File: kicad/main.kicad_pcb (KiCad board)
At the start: 2 copper layers, 13 parts, among them J1 Conn_02x14_Counter_Clockwise, U1 7421, U2 74LS86, U3 74LS138, U4 7421, U5 7421, U6 74LS138

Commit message: started layout for multiplexer
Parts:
- moved C4 114.3 mm to (281.9, 76.2)
- moved C2 112.3 mm to (282.0, 99.1)
- moved C1 110.8 mm to (282.0, 85.1)
- moved C3 110.1 mm to (282.0, 92.7)
- moved C5 109.4 mm to (282.0, 106.7)
- moved C6 109.3 mm to (282.0, 111.8)
- moved U6 108.5 mm to (76.9, 160.3), turned to -90 degrees
- moved U3 90.2 mm to (59.2, 155.2), turned to 90 degrees
- moved J1 73.1 mm to (43.2, 97.8), turned to 180 degrees
- moved U5 43.2 mm to (129.5, 91.4)
- moved U4 22.6 mm to (129.5, 58.4)
- moved U1 19.0 mm to (147.3, 73.7)
- moved U2 6.85 mm to (86.4, 76.2)
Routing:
- net +5V: track 0.00 -> 70.0 mm
- net GND: track 0.00 -> 68.9 mm, vias 0 -> 1
- net /adressInverter//PWM: track 0.00 -> 56.4 mm
- net /adressInverter/H3_OUT: track 0.00 -> 46.6 mm
- net /adressInverter/H1_OUT: track 0.00 -> 35.1 mm
- net Net-(U6-~{Y6}): track 0.00 -> 26.1 mm
- net /adressInverter/H2_OUT: track 0.00 -> 25.6 mm
- net Net-(U6-~{Y5}): track 0.00 -> 23.9 mm
- net Net-(U6-~{Y4}): track 0.00 -> 21.6 mm
- net unconnected-(U3-~{Y0}-Pad15): track 0.00 -> 20.4 mm
- net Net-(U6-~{Y3}): track 0.00 -> 18.8 mm
- net Net-(U3-~{Y1}): track 0.00 -> 16.3 mm
- net /PWM_IN: track 0.00 -> 16.2 mm
- net Net-(U6-~{Y2}): track 0.00 -> 14.0 mm
- net Net-(U3-~{Y2}): track 0.00 -> 13.4 mm
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
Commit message: finished individual components layouts
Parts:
- moved C2 223.7 mm to (58.5, 88.9)
- moved C4 169.5 mm to (118.1, 119.7), turned to -90 degrees
- moved C1 153.2 mm to (141.0, 145.0)
- moved C6 126.7 mm to (163.8, 66.1), turned to 180 degrees
- moved C3 103.8 mm to (181.6, 66.0), turned to 180 degrees
- moved C5 92.0 mm to (199.4, 66.0)
- moved U5 68.2 mm to (191.8, 63.5), turned to 180 degrees
- moved U3 66.5 mm to (120.7, 129.8)
- moved U6 66.5 mm to (138.4, 134.9)
- moved U1 63.1 mm to (209.6, 63.5), turned to 180 degrees
- moved U4 44.7 mm to (174.0, 63.5), turned to 180 degrees
- moved U2 22.7 mm to (66.0, 86.4), turned to 180 degrees
- moved J1 10.5 mm to (53.3, 95.3)
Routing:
- net GND: track 68.9 -> 195.1 mm
- net +5V: track 70.0 -> 185.5 mm
- net Net-(U6-~{Y3}): track 18.8 -> 112.7 mm
- net /G_L_OUT: track 0.00 -> 72.9 mm
- net Net-(U3-~{Y5}): track 4.57 -> 71.8 mm
- net Net-(U3-~{Y4}): track 7.49 -> 70.2 mm
- net Net-(U6-~{Y2}): track 14.0 -> 71.6 mm
- net /B_L_OUT: track 0.00 -> 55.5 mm
- net /Y_H_OUT: track 0.00 -> 51.2 mm
- net Net-(U3-~{Y2}): track 13.4 -> 61.3 mm
- net Net-(U6-~{Y5}): track 23.9 -> 71.1 mm
- net Net-(U3-~{Y6}): track 4.42 -> 49.8 mm
- net Net-(U6-~{Y1}): track 11.2 -> 42.9 mm
- net /PWM_IN: track 16.2 -> 43.4 mm
- net /H1_IN: track 0.00 -> 23.6 mm
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
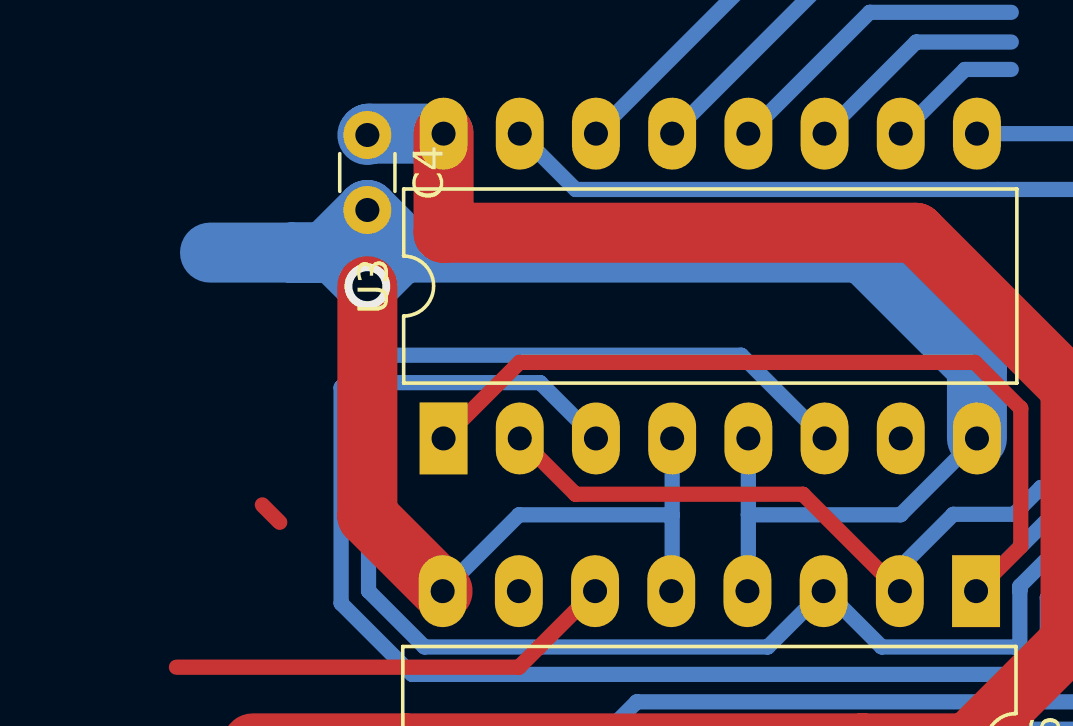
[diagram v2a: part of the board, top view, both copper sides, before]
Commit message: deleted unnecessary complexity
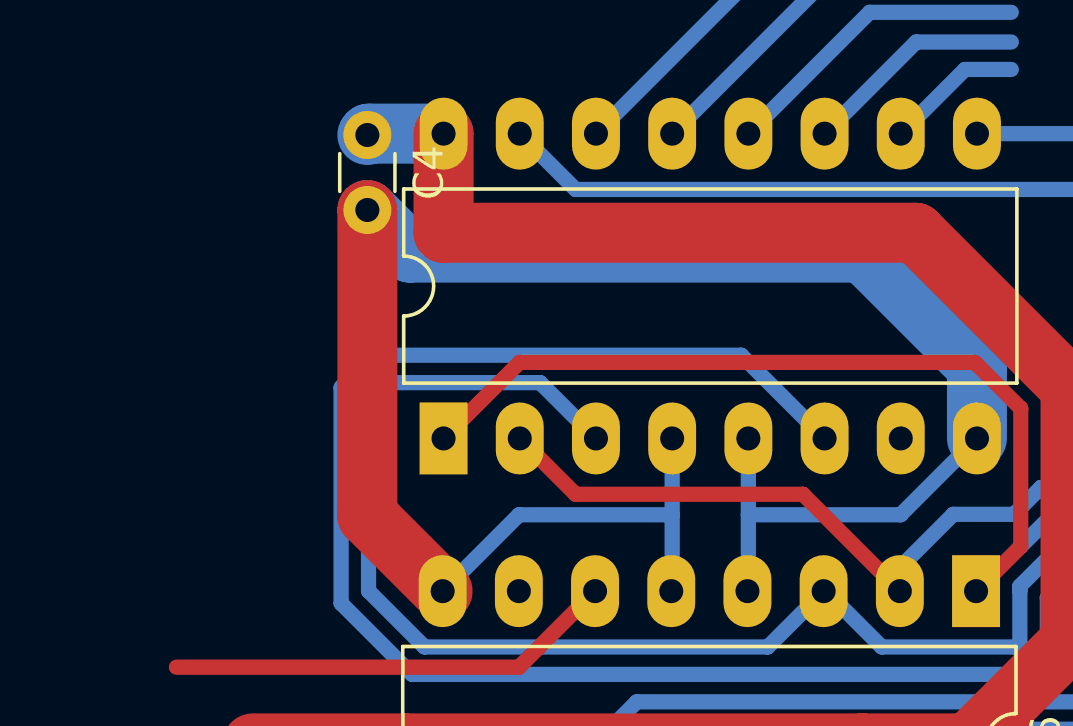
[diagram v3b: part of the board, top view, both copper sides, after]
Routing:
- net GND: track 195.1 -> 187.0 mm, vias 1 -> 0
- net /PWM_IN: track 43.4 -> 42.5 mm
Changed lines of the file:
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@@
     (property "Sheetname" "com_dmux")
     (attr through_hole)
-    (fp_text reference "U3" (at 5.08 -2.33 90) (layer "F.SilkS")
+    (fp_text reference "U3" (at 5.08 -2.33 90) (layer "F.SilkS") hide
         (effects (font (size 1 1) (thickness 0.15)))
     )
@@
   (segment (start 181.62 66.045) (end 181.62 66.665321) (width 2) (layer "B.Cu") (net 1))
   (segment (start 140.981578 145.0248) (end 140.986578 145.0198) (width 2) (layer "B.Cu") (net 1))
-  (segment (start 118.126578 124.6998) (end 118.126578 132.3548) (width 2) (layer "F.Cu") (net 2))
   (segment (start 177.299999 58.44) (end 177.299999 49.224999) (width 2) (layer "F.Cu") (net 2))
+  (segment (start 118.126578 122.1598) (end 118.126578 132.3548) (width 2) (layer "F.Cu") (net 2))
   (segment (start 179.12 66.045) (end 177.299999 64.224999) (width 2) (layer "F.Cu") (net 2))
   (segment (start 118.126578 132.3548) (end 120.636578 134.8648) (width 2) (layer "F.Cu") (net 2))
@@
   (segment (start 176.54 48.465) (end 174 48.465) (width 2) (layer "F.Cu") (net 2))
   (segment (start 177.299999 49.224999) (end 176.54 48.465) (width 2) (layer "F.Cu") (net 2))
-  (via (at 118.126578 124.6998) (size 1.524) (drill 1) (layers "F.Cu" "B.Cu") (net 2))
   (segment (start 201.94 46.0536) (end 202.0014 46.115) (width 2) (layer "B.Cu") (net 2))
   (segment (start 63.1096 84.50776) (end 63.1096 73.060079) (width 2) (layer "B.Cu") (net 2))
-  (segment (start 119.246578 123.2798) (end 119.246578 123.5798) (width 2) (layer "B.Cu") (net 2))
   (segment (start 201.94 46.0536) (end 207.3436 46.0536) (width 2) (layer "B.Cu") (net 2))
+  (segment (start 118.126578 122.1598) (end 119.546578 123.5798) (width 2) (layer "B.Cu") (net 2))
   (segment (start 66.03 86.36) (end 64.96184 86.36) (width 2) (layer "B.Cu") (net 2))
   (segment (start 193.9764 46.0536) (end 201.94 46.0536) (width 2) (layer "B.Cu") (net 2))
-  (segment (start 115.586578 123.5798) (end 112.881578 123.5798) (width 2) (layer "B.Cu") (net 2))
   (segment (start 130.826578 132.3198) (end 130.826578 134.8348) (width 0.508) (layer "B.Cu") (net 2))
   (segment (start 60.96 88.9) (end 63.1096 86.7504) (width 2) (layer "B.Cu") (net 2))
@@
   (segment (start 57.155 62.245) (end 66.03 71.12) (width 2) (layer "B.Cu") (net 2))
   (segment (start 64.716079 71.4536) (end 66.04 71.4536) (width 2) (layer "B.Cu") (net 2))
-  (segment (start 118.126578 122.1598) (end 119.246578 123.2798) (width 2) (layer "B.Cu") (net 2))
   (segment (start 128.286578 129.7748) (end 128.286578 132.3198) (width 0.508) (layer "B.Cu") (net 2))
   (segment (start 176.1964 46.0686) (end 174 48.265) (width 2) (layer "B.Cu") (net 2))
@@
   (segment (start 135.901578 132.3198) (end 130.826578 132.3198) (width 0.508) (layer "B.Cu") (net 2))
   (segment (start 134.651578 123.5798) (end 138.446578 127.3748) (width 2) (layer "B.Cu") (net 2))
-  (segment (start 118.126578 122.1598) (end 116.706578 123.5798) (width 2) (layer "B.Cu") (net 2))
+  (segment (start 119.546578 123.5798) (end 134.651578 123.5798) (width 2) (layer "B.Cu") (net 2))
   (segment (start 191.77 48.26) (end 189.5636 46.0536) (width 2) (layer "B.Cu") (net 2))
   (segment (start 120.636578 134.8648) (end 123.181578 132.3198) (width 0.508) (layer "B.Cu") (net 2))
-  (segment (start 116.706578 123.5798) (end 115.586578 123.5798) (width 2) (layer "B.Cu") (net 2))
   (segment (start 63.1096 73.060079) (end 64.716079 71.4536) (width 2) (layer "B.Cu") (net 2))
   (segment (start 128.286578 132.3198) (end 128.286578 134.8348) (width 0.508) (layer "B.Cu") (net 2))
-  (segment (start 118.126578 124.6998) (end 119.246578 123.5798) (width 2) (layer "B.Cu") (net 2))
   (segment (start 202.0014 46.115) (end 202.0014 65.9436) (width 2) (layer "B.Cu") (net 2))
   (segment (start 189.5636 46.0536) (end 176.1964 46.0536) (width 2) (layer "B.Cu") (net 2))
-  (segment (start 117.006578 123.5798) (end 115.586578 123.5798) (width 2) (layer "B.Cu") (net 2))
-  (segment (start 118.126578 124.6998) (end 117.006578 123.5798) (width 2) (layer "B.Cu") (net 2))
   (segment (start 191.77 48.26) (end 193.9764 46.0536) (width 2) (layer "B.Cu") (net 2))
   (segment (start 138.446578 129.7748) (end 135.901578 132.3198) (width 0.508) (layer "B.Cu") (net 2))
@@
   (segment (start 64.96184 86.36) (end 63.1096 84.50776) (width 2) (layer "B.Cu") (net 2))
   (segment (start 53.345 62.245) (end 57.155 62.245) (width 2) (layer "B.Cu") (net 2))
-  (segment (start 119.246578 123.5798) (end 134.651578 123.5798) (width 2) (layer "B.Cu") (net 2))
   (segment (start 207.3436 46.0536) (end 209.55 48.26) (width 2) (layer "B.Cu") (net 2))
   (segment (start 202.0014 65.9436) (end 201.9 66.045) (width 2) (layer "B.Cu") (net 2))
@@
   (segment (start 123.856178 136.7252) (end 123.181578 137.3998) (width 0.508) (layer "F.Cu") (net 8))
   (segment (start 66.938 83.82) (end 66.03 83.82) (width 0.508) (layer "F.Cu") (net 8))
-  (segment (start 115.206778 132.5704) (end 114.626378 131.99) (width 0.508) (layer "F.Cu") (net 8))
   (segment (start 125.716578 134.8648) (end 125.716578 134.4648) (width 0.508) (layer "F.Cu") (net 8))
   (segment (start 56.5496 89.054918) (end 58.055082 90.5604) (width 0.508) (layer "B.Cu") (net 8))

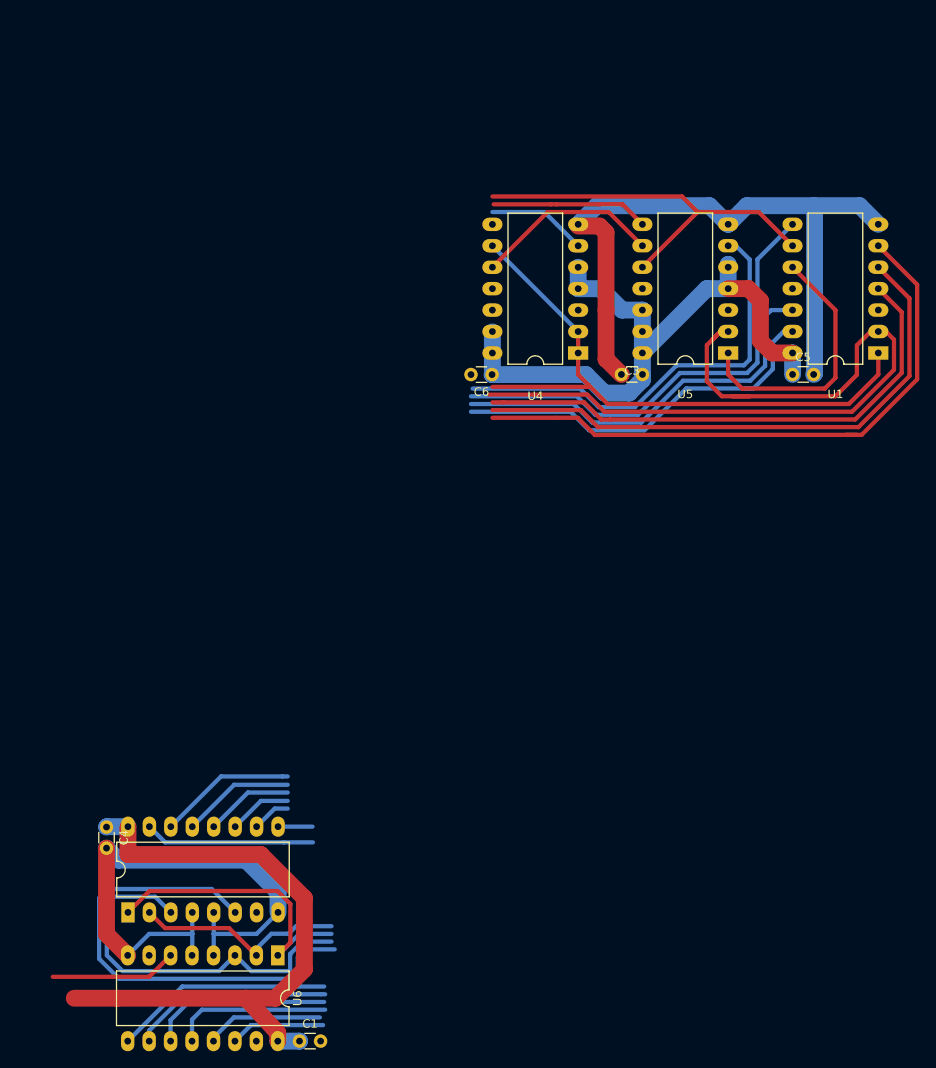
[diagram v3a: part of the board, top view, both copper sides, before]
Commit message: fixed unreachable pin
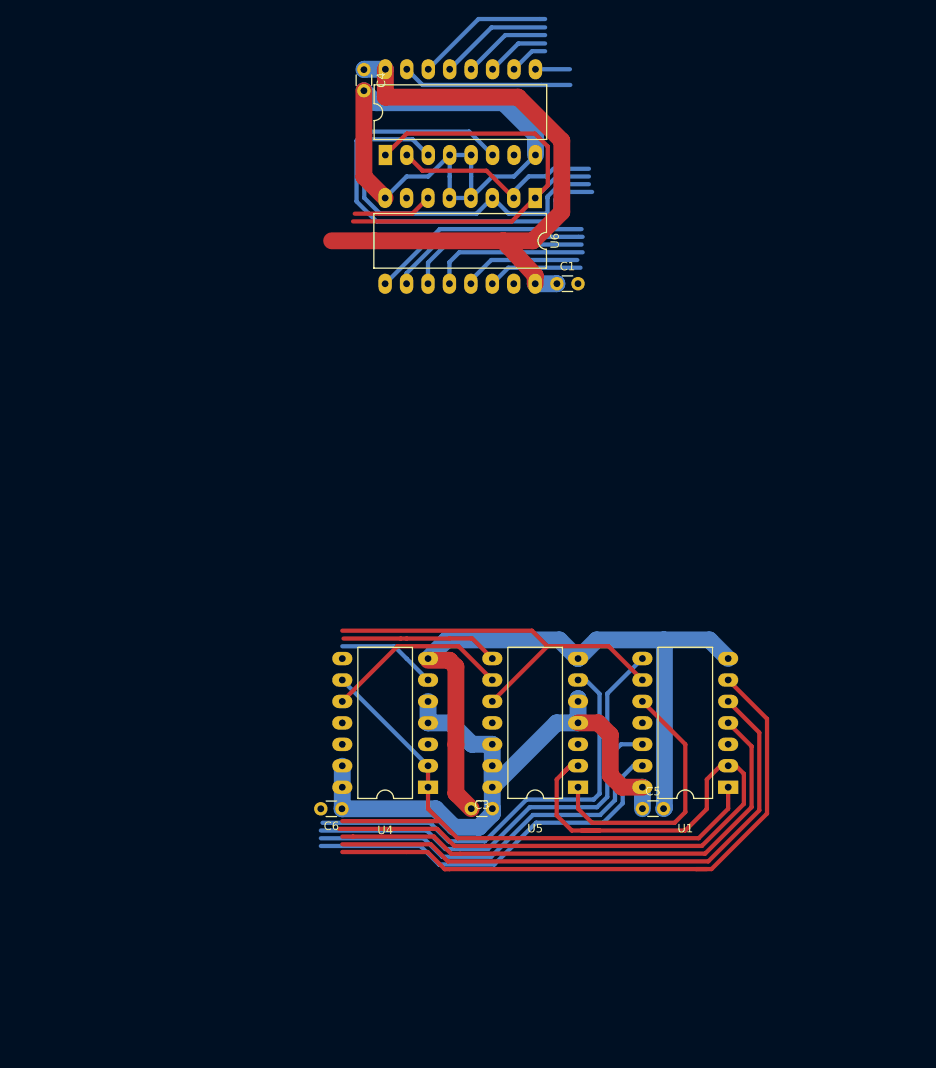
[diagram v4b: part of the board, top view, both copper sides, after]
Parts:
- moved C4 94.8 mm to (148.6, 29.9)
- moved U6 94.8 mm to (168.9, 45.1)
- moved C1 94.8 mm to (171.5, 55.3)
- moved U3 94.8 mm to (151.2, 40.0)
- moved C6 54.4 mm to (146.0, 117.5)
- moved C3 54.4 mm to (163.8, 117.5)
- moved C5 54.4 mm to (181.6, 117.5)
- moved U1 54.4 mm to (191.8, 114.9)
- moved U5 54.4 mm to (174.0, 114.9)
- moved U4 54.4 mm to (156.2, 114.9)
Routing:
- net /adressInverter/H1_OUT: track 35.1 -> 57.8 mm
- net GND: track 187.0 -> 194.3 mm
- net /PWM_IN: track 42.5 -> 37.0 mm

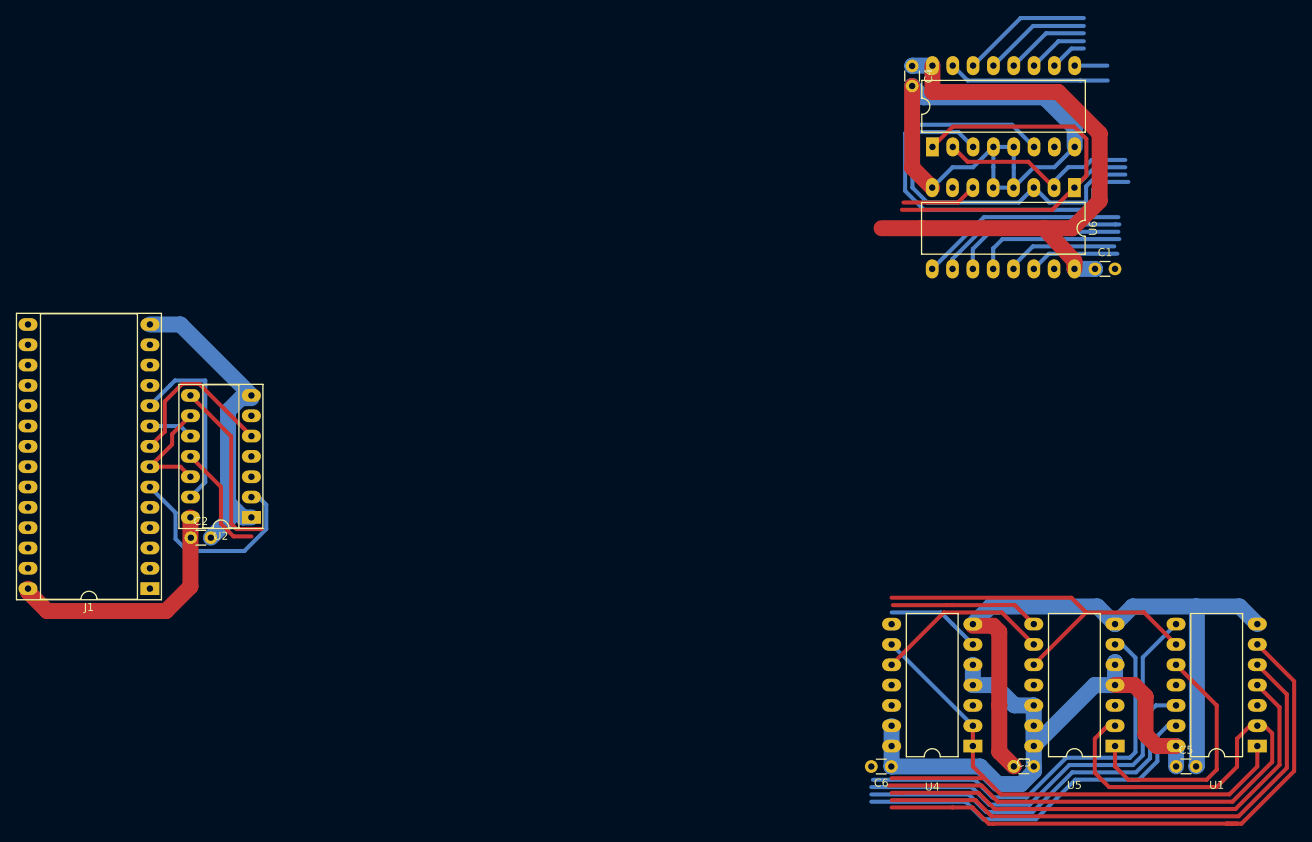
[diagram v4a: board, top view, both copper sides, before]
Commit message: changed orientation of plug
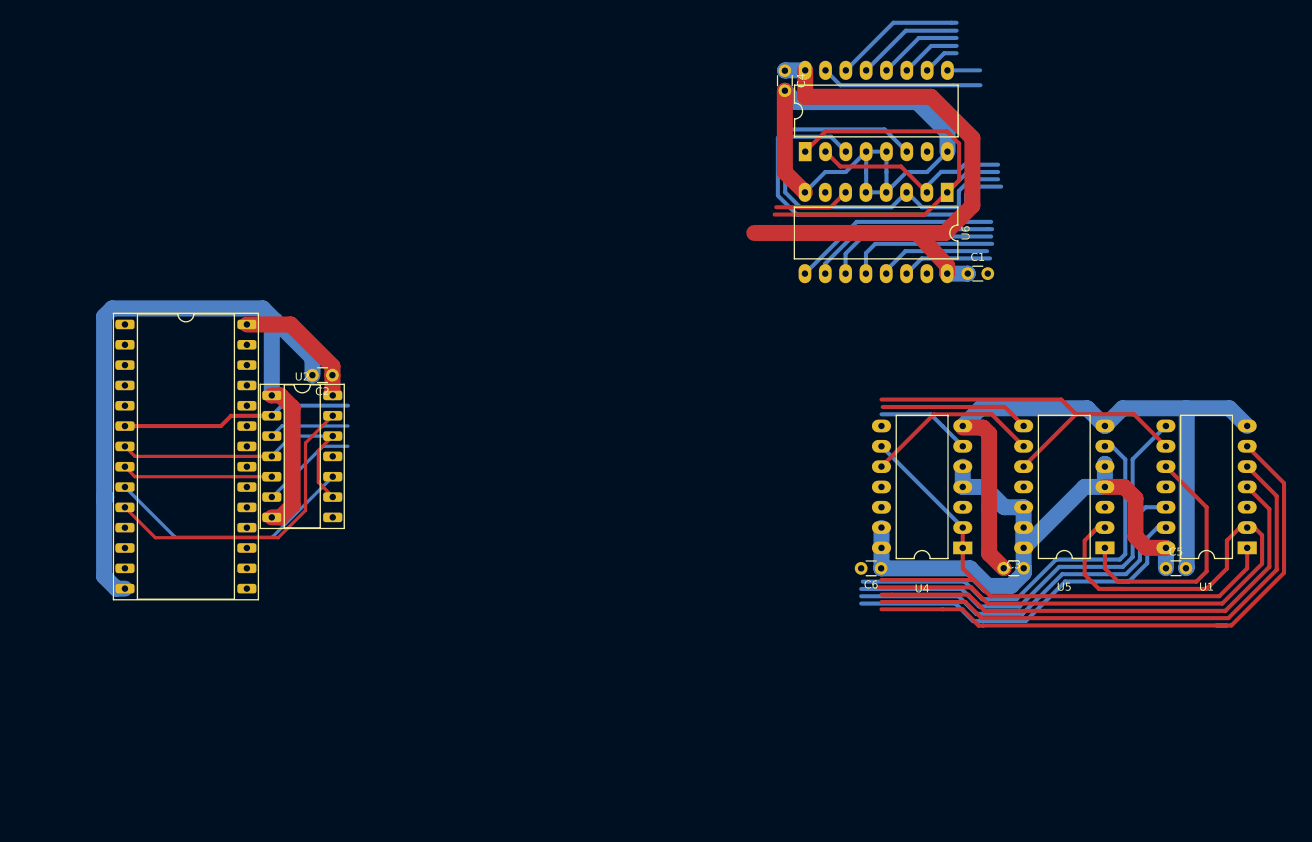
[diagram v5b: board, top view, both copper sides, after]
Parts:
- moved J1 33.2 mm to (50.2, 62.2), turned to 0 degrees
- moved C2 26.9 mm to (76.2, 68.6), turned to 180 degrees
- moved C3 24.8 mm to (162.6, 92.7)
- moved C5 24.8 mm to (180.3, 92.7)
- moved U1 24.8 mm to (190.5, 90.2)
- moved U4 24.8 mm to (154.9, 90.2)
- moved U5 24.8 mm to (172.7, 90.2)
- moved C6 24.8 mm to (144.8, 92.7)
- moved C1 15.9 mm to (155.6, 55.9)
- moved C4 15.9 mm to (132.7, 30.5)
- moved U3 15.9 mm to (135.3, 40.6)
- moved U6 15.9 mm to (153.0, 45.7)
- moved U2 15.5 mm to (68.6, 71.1), turned to 0 degrees
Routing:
- net GND: track 194.3 -> 249.3 mm
- net /H2_IN: track 5.60 -> 31.7 mm
- net /DIR_IN: track 14.0 -> 36.7 mm
- net /adressInverter/H2_OUT: track 47.8 -> 25.6 mm
- net +5V: track 185.5 -> 170.0 mm
- net /H1_IN: track 23.6 -> 38.8 mm
- net /adressInverter/H3_OUT: track 61.1 -> 46.6 mm
- net /adressInverter/H1_OUT: track 57.8 -> 69.9 mm
- net /adressInverter//PWM: track 56.4 -> 66.5 mm
- net /H3_IN: track 20.8 -> 18.9 mm
- net /PWM_IN: track 37.0 -> 38.8 mm
